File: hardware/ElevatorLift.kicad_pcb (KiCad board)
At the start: 2 copper layers, 0 parts

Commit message: Capture confirmed hardware constraints and KiCad 10 scaffold
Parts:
- added H1: MountingHole_3.2mm_M3, MountingHole_3.2mm_M3, F.Cu at (6.35, 6.35)
- added H2: MountingHole_3.2mm_M3, MountingHole_3.2mm_M3, F.Cu at (82.5, 6.35)
- added H3: MountingHole_3.2mm_M3, MountingHole_3.2mm_M3, F.Cu at (82.5, 82.5)
- added H4: MountingHole_3.2mm_M3, MountingHole_3.2mm_M3, F.Cu at (6.35, 82.5)
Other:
- board outline added: 88.9 x 88.9 mm
- board text added: "A0 placeholder outline: 3.5 in x 3.5 in"

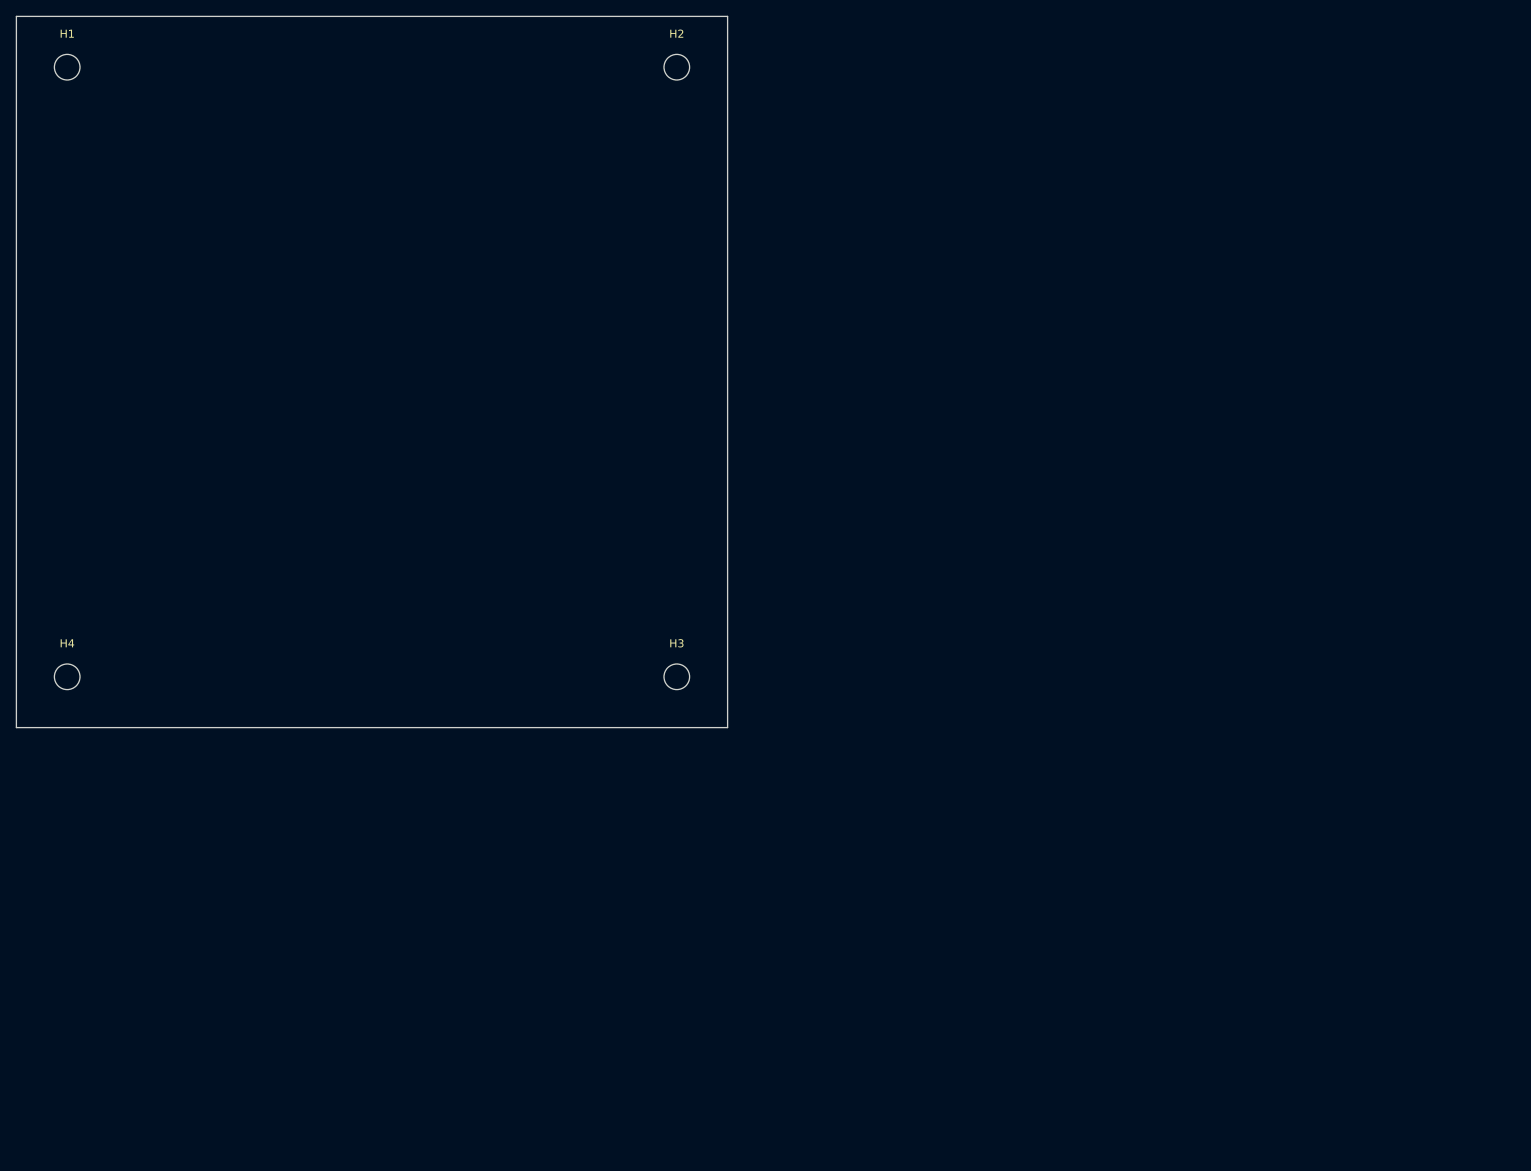
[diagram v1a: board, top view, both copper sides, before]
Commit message: Capture portable Rev-A hardware design
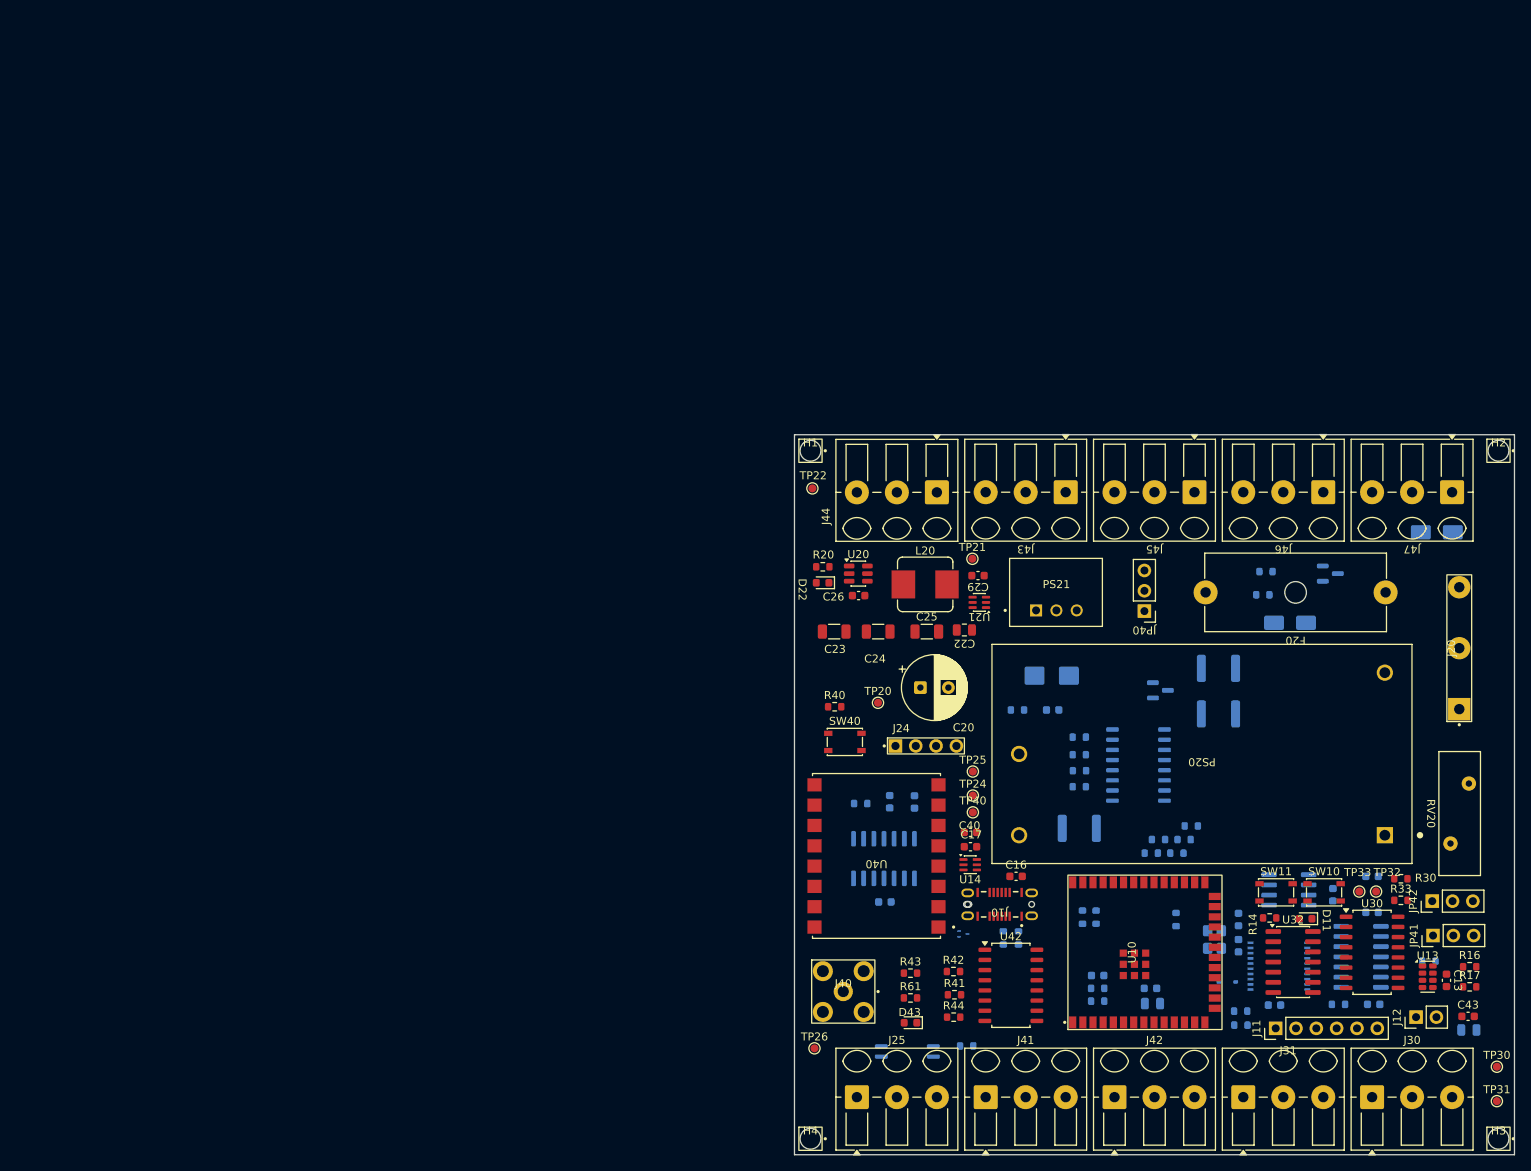
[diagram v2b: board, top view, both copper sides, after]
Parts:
- added C11: 100nF MRAM decoupling, Capacitor_SMD:C_0603_1608Metric, B.Cu at (164.6, 109.8)
- added C12: 1uF EN reset delay, Capacitor_SMD:C_0603_1608Metric, B.Cu at (135.2, 119.9)
- added C13: 100nF RTC decoupling, Capacitor_SMD:C_0603_1608Metric, F.Cu at (178.8, 120.5)
- added C14: 100nF ESP32 decoupling, Capacitor_SMD:C_0603_1608Metric, B.Cu at (141.8, 121.5)
- added C15: 10uF ESP32 bulk, Capacitor_SMD:C_0805_2012Metric, B.Cu at (142.0, 123.4)
- added C16: 1u USB IN, Capacitor_SMD:C_0603_1608Metric, F.Cu at (125.0, 107.5)
- added C17: 1u 5V OUT, Capacitor_SMD:C_0603_1608Metric, F.Cu at (119.3, 103.8)
- added C20: 100u 25V, Capacitor_THT:CP_Radial_D8.0mm_P3.50mm, F.Cu at (113.0, 83.9)
- added C21: 100n 25V, Capacitor_SMD:C_0603_1608Metric, B.Cu at (129.5, 86.7)
- added C22: 10u 10V, Capacitor_SMD:C_0805_2012Metric, F.Cu at (118.5, 76.7)
- added C23: 10u 25V, Capacitor_SMD:C_1206_3216Metric, F.Cu at (102.2, 76.9)
- added C24: 22u 10V, Capacitor_SMD:C_1206_3216Metric, F.Cu at (107.7, 76.9)
- added C25: 22u 10V, Capacitor_SMD:C_1206_3216Metric, F.Cu at (113.8, 76.9)
- added C26: 100n BST, Capacitor_SMD:C_0603_1608Metric, F.Cu at (105.3, 72.4)
- added C27: 100n 3V3, Capacitor_SMD:C_0603_1608Metric, B.Cu at (109.2, 98.2)
- added C28: 100n 5V, Capacitor_SMD:C_0603_1608Metric, B.Cu at (112.3, 98.2)
- added C29: 1uF, Capacitor_SMD:C_0603_1608Metric, F.Cu at (120.2, 69.9)
- added C30: 18pF, Capacitor_SMD:C_0603_1608Metric, B.Cu at (152.8, 116.2)
- added C31: 18pF, Capacitor_SMD:C_0603_1608Metric, B.Cu at (152.8, 112.9)
- added C32: 100nF LS7366R decoupling, Capacitor_SMD:C_0603_1608Metric, B.Cu at (157.3, 123.6)
- added C33: 100nF 74HC14 decoupling, Capacitor_SMD:C_0603_1608Metric, B.Cu at (169.7, 123.5)
- added C34: 100nF 12V FIELD DECOUPLING, Capacitor_SMD:C_0603_1608Metric, B.Cu at (169.5, 107.5)
- added C40: 100n, Capacitor_SMD:C_0603_1608Metric, F.Cu at (119.3, 102.0)
- added C41: 100n, Capacitor_SMD:C_0603_1608Metric, B.Cu at (108.6, 110.7)
- added C42: 100n, Capacitor_SMD:C_0603_1608Metric, B.Cu at (169.5, 112.0)
- added C43: 100n, Capacitor_SMD:C_0603_1608Metric, F.Cu at (181.5, 125.0)
- added C44: 10u, Capacitor_SMD:C_0805_2012Metric, B.Cu at (181.6, 126.7)
- added D11: GREEN STATUS, LED_SMD:LED_0603_1608Metric, F.Cu at (161.2, 112.8)
- added D20: SMBJ15A, Diode_SMD:D_SMB, B.Cu at (129.4, 82.4)
- added D22: 3V3 OK, LED_SMD:LED_0603_1608Metric, F.Cu at (100.8, 70.8)
- added D40: BAT54, Diode_SMD:D_SOD-323, B.Cu at (151.4, 120.7)
- added D41: SMBJ15A, Diode_SMD:D_SMA, B.Cu at (159.2, 75.8)
- added D42: SMBJ15A, Diode_SMD:D_SMA, B.Cu at (177.6, 64.5)
- added D43: RF MODE, LED_SMD:LED_0603_1608Metric, F.Cu at (111.8, 125.8)
- added F20: T500mA 250VAC + 0031.8201, Fuse:Fuseholder_Cylinder-5x20mm_Schurter_0031_8201_Horizontal_Open, F.Cu at (171.2, 72.0)
- added F21: 0.75A PTC, Fuse:Fuse_1812_4532Metric, B.Cu at (132.9, 101.5)
- added F40: 1.1A HOLD, Fuse:Fuse_1812_4532Metric, B.Cu at (150.3, 81.5)
- added F41: 500mA HOLD, Fuse:Fuse_1812_4532Metric, B.Cu at (150.3, 87.2)
- added J10: USB4145-03-0230-C_REVA2, SnapEDA:GCT_USB4145-03-0230-C_REVA2, F.Cu at (122.9, 111.0)
- added J11: UART RECOVERY / BOOT, Connector_PinHeader_2.54mm:PinHeader_1x06_P2.54mm_Vertical, F.Cu at (157.4, 126.5)
- added J12: RTC BACKUP 3V, Connector_PinHeader_2.54mm:PinHeader_1x02_P2.54mm_Vertical, F.Cu at (175.0, 125.1)
- added J20: Phoenix 1717732 GMKDS 1,5/3-7,62 MAINS L/N/PE, ElevatorLift_Custom:Phoenix_GMKDS-1.5-3-7.62_1717732_Provisional, F.Cu at (180.4, 79.0)
- added J24: VFD UART 5V GND RX TX, ElevatorLift_Custom:SAMTEC_TSW-104-07-G-S_ZeroPadded, F.Cu at (113.7, 91.2)
- added J25: ED300/3 VFD RUN C / E / SPARE, TerminalBlock_Altech:Altech_AK300_1x03_P5.00mm_45-Degree, F.Cu at (105.1, 135.1)
- added J30: ENCODER A: +12V GND A, TerminalBlock_Altech:Altech_AK300_1x03_P5.00mm_45-Degree, F.Cu at (169.5, 135.1)
- added J31: ENCODER B: +12V GND B, TerminalBlock_Altech:Altech_AK300_1x03_P5.00mm_45-Degree, F.Cu at (153.4, 135.1)
- added J40: CONSMA002 (418 MHz ANT), ElevatorLift_Custom:SMA_TE-Linx_CONSMA002_RightAngle, F.Cu at (103.4, 121.9)
- added J41: ED300/3 SAFETY HOME GND, TerminalBlock_Altech:Altech_AK300_1x03_P5.00mm_45-Degree, F.Cu at (121.2, 135.1)
- added J42: ED300/3 LIMIT UP DOWN GND, TerminalBlock_Altech:Altech_AK300_1x03_P5.00mm_45-Degree, F.Cu at (137.3, 135.1)
- added J43: ED300/3 SERVICE KEY HOLD GND, TerminalBlock_Altech:Altech_AK300_1x03_P5.00mm_45-Degree, F.Cu at (131.2, 59.5)
- added J44: ED300/3 SERVICE UP DOWN GND, TerminalBlock_Altech:Altech_AK300_1x03_P5.00mm_45-Degree, F.Cu at (115.1, 59.5)
- added J45: ED300/3 EXT LIGHT 12V / GND / SPARE, TerminalBlock_Altech:Altech_AK300_1x03_P5.00mm_45-Degree, F.Cu at (147.3, 59.5)
- added J46: ED300/3 LIGHT + / SW- / GND, TerminalBlock_Altech:Altech_AK300_1x03_P5.00mm_45-Degree, F.Cu at (163.4, 59.5)
- added J47: ED300/3 AUX + / SW- / GND, TerminalBlock_Altech:Altech_AK300_1x03_P5.00mm_45-Degree, F.Cu at (179.5, 59.5)
- added JP40: LIGHT SUPPLY SELECT, Connector_PinHeader_2.54mm:PinHeader_1x03_P2.54mm_Vertical, F.Cu at (141.0, 74.3)
- added JP41: RF BAUD0 SELECT, Connector_PinHeader_2.54mm:PinHeader_1x03_P2.54mm_Vertical, F.Cu at (177.1, 114.9)
- added JP42: RF BAUD1 SELECT, Connector_PinHeader_2.54mm:PinHeader_1x03_P2.54mm_Vertical, F.Cu at (177.0, 110.6)
- added L20: 2.2uH, Inductor_SMD:L_Bourns_SRP7028A_7.3x6.6mm, F.Cu at (113.6, 71.0)
- added PS20: RAC10-12SK/277, SnapEDA:CONV_RAC10-12SK_277, F.Cu at (148.2, 92.2)
- added PS21: R-78E5.0-0.5, SnapEDA:CONV_R-78E5.0-0.5, F.Cu at (130.0, 72.0)
- added Q40: AO3400A, Package_TO_SOT_SMD:SOT-23, B.Cu at (164.2, 69.7)
- added Q41: AO3400A, Package_TO_SOT_SMD:SOT-23, B.Cu at (143.0, 84.2)
- added R10: 5.1k 1% CC1, Resistor_SMD:R_0603_1608Metric, B.Cu at (123.4, 115.2)
- added R11: 5.1k 1% CC2, Resistor_SMD:R_0603_1608Metric, B.Cu at (125.3, 115.2)
- added R12: 10k EN pull-up, Resistor_SMD:R_0603_1608Metric, B.Cu at (135.2, 121.5)
- added R13: 10k BOOT pull-up, Resistor_SMD:R_0603_1608Metric, B.Cu at (146.9, 101.2)
- added R14: 1k STATUS LED, Resistor_SMD:R_0603_1608Metric, F.Cu at (156.7, 112.7)
- added R16: 4.7k I2C SDA pull-up, Resistor_SMD:R_0603_1608Metric, F.Cu at (181.7, 118.8)
- added R17: 4.7k I2C SCL pull-up, Resistor_SMD:R_0603_1608Metric, F.Cu at (181.7, 121.3)
- added R20: 1k, Resistor_SMD:R_0603_1608Metric, F.Cu at (100.8, 68.8)
- added R21: 0R, Resistor_SMD:R_0603_1608Metric, B.Cu at (125.1, 86.7)
- added R24: 10k OE pull-down, Resistor_SMD:R_0603_1608Metric, B.Cu at (105.5, 98.4)
- added R25: 680R, Resistor_SMD:R_0603_1608Metric, B.Cu at (118.8, 128.7)
- added R30: 2.2k ENCODER A LED, Resistor_SMD:R_0603_1608Metric, F.Cu at (173.1, 107.8)
- added R31: 2.2k ENCODER B LED, Resistor_SMD:R_0603_1608Metric, B.Cu at (176.6, 118.1)
- added R32: 10k A pull-up, Resistor_SMD:R_0603_1608Metric, B.Cu at (165.3, 123.5)
- added R33: 10k B pull-up, Resistor_SMD:R_0603_1608Metric, F.Cu at (173.1, 110.5)
- added R40: 100k, Resistor_SMD:R_0603_1608Metric, F.Cu at (102.3, 86.3)
- added R41: 2.2k, Resistor_SMD:R_0603_1608Metric, F.Cu at (117.3, 122.3)
- added R42: 2.2k, Resistor_SMD:R_0603_1608Metric, F.Cu at (117.1, 119.4)
- added R43: 2.2k, Resistor_SMD:R_0603_1608Metric, F.Cu at (111.8, 119.6)
- added R44: 2.2k, Resistor_SMD:R_0603_1608Metric, F.Cu at (117.2, 125.1)
- added R45: 2.2k, Resistor_SMD:R_0603_1608Metric, B.Cu at (132.9, 96.3)
- added R46: 2.2k, Resistor_SMD:R_0603_1608Metric, B.Cu at (132.9, 94.3)
- added R47: 2.2k, Resistor_SMD:R_0603_1608Metric, B.Cu at (132.9, 92.3)
- added R48: 2.2k, Resistor_SMD:R_0603_1608Metric, B.Cu at (132.9, 90.1)
- added R49: 10k, Resistor_SMD:R_0603_1608Metric, B.Cu at (133.3, 112.6)
- added R50: 10k, Resistor_SMD:R_0603_1608Metric, B.Cu at (135.0, 112.6)
- added R51: 10k, Resistor_SMD:R_0603_1608Metric, B.Cu at (145.0, 112.9)
- added R52: 10k, Resistor_SMD:R_0603_1608Metric, B.Cu at (135.2, 123.1)
- added R53: 10k, Resistor_SMD:R_0603_1608Metric, B.Cu at (146.0, 102.9)
- added R54: 10k, Resistor_SMD:R_0603_1608Metric, B.Cu at (145.1, 104.6)
- added R55: 10k, Resistor_SMD:R_0603_1608Metric, B.Cu at (142.8, 102.9)
- added R56: 10k, Resistor_SMD:R_0603_1608Metric, B.Cu at (141.9, 104.6)
- added R57: 100R, Resistor_SMD:R_0603_1608Metric, B.Cu at (155.8, 72.3)
- added R58: 100k, Resistor_SMD:R_0603_1608Metric, B.Cu at (156.2, 69.4)
- added R59: 100R, Resistor_SMD:R_0603_1608Metric, B.Cu at (153.0, 124.3)
- added R60: 100k, Resistor_SMD:R_0603_1608Metric, B.Cu at (153.1, 126.1)
- added R61: 1k, Resistor_SMD:R_0603_1608Metric, F.Cu at (111.8, 122.7)
- added RV20: Bourns MOV-14D241K, Varistor:RV_Disc_D15.5mm_W5.2mm_P7.5mm, F.Cu at (181.6, 95.9)
- added SW10: RESET, Button_Switch_SMD:SW_SPST_PTS810, F.Cu at (163.5, 109.5)
- added SW11: BOOT, Button_Switch_SMD:SW_SPST_PTS810, F.Cu at (157.5, 109.5)
- added SW40: RF LEARN, Button_Switch_SMD:SW_SPST_PTS810, F.Cu at (103.6, 90.7)
- added TP20: +12V TEST, TestPoint:TestPoint_Pad_D1.0mm, F.Cu at (107.7, 85.8)
- added TP21: +5V TEST, TestPoint:TestPoint_Pad_D1.0mm, F.Cu at (119.5, 67.8)
- added TP22: +3V3 TEST, TestPoint:TestPoint_Pad_D1.0mm, F.Cu at (99.5, 59.0)
- added TP24: VFD RX 5V, TestPoint:TestPoint_Pad_D1.0mm, F.Cu at (119.6, 97.4)
- added TP25: VFD TX 5V, TestPoint:TestPoint_Pad_D1.0mm, F.Cu at (119.6, 94.4)
- added TP26: VFD RUN COLLECTOR, TestPoint:TestPoint_Pad_D1.0mm, F.Cu at (99.8, 129.0)
- added TP30: ENC_A_FIELD, TestPoint:TestPoint_Pad_D1.0mm, F.Cu at (185.1, 131.3)
- added TP31: ENC_B_FIELD, TestPoint:TestPoint_Pad_D1.0mm, F.Cu at (185.1, 135.6)
- added TP32: ENC_A_CLEAN, TestPoint:TestPoint_Pad_D1.0mm, F.Cu at (170.0, 109.4)
- added TP33: ENC_B_CLEAN, TestPoint:TestPoint_Pad_D1.0mm, F.Cu at (167.9, 109.4)
- added TP40: RF RSSI, TestPoint:TestPoint_Pad_D1.0mm, F.Cu at (119.6, 99.5)
- added U10: ESP32-S3-WROOM-1U-N16R8, ElevatorLift_Custom:ESP32-S3-WROOM-1U-N16R8_CorrectedV2, F.Cu at (140.4, 117.0)
- added U11: PM004MNIATR 4Mbit MRAM, Package_SO:SOIC-8_3.9x4.9mm_P1.27mm, B.Cu at (159.1, 109.2)
- added U12: TPD2EUSB30ADRTR USB ESD, SnapEDA:SOTFL35P100X50-3N, B.Cu at (118.4, 114.7)
- added U13: RV-3028-C7 RTC, Package_SON:MicroCrystal_C7_SON-8_1.5x3.2mm_P0.9mm, F.Cu at (176.4, 120.0)
- added U14: LM66100DCKR USB IDEAL DIODE, Package_TO_SOT_SMD:SOT-363_SC-70-6, F.Cu at (119.2, 106.0)
- added U20: AP63203WU 3V3 2A, Package_TO_SOT_SMD:TSOT-23-6, F.Cu at (105.2, 69.7)
- added U21: LM66100DCKR, Package_TO_SOT_SMD:SOT-363_SC-70-6, F.Cu at (120.4, 73.2)
- added U24: TXS0104ED (3V3 <-> 5V), Package_SO:SOIC-14_3.9x8.7mm_P1.27mm, B.Cu at (108.5, 105.3)
- added U25: VFD RUN OPEN COLLECTOR, Package_SO:SOIC-4_4.55x2.6mm_P1.27mm, B.Cu at (111.4, 129.4)
- added U30: TLP291-4 ENCODER ISOLATION, Package_SO:SOIC-16_4.55x10.3mm_P1.27mm, F.Cu at (169.5, 117.0)
- added U31: 74HC14D SCHMITT CONDITIONING, Package_SO:SOIC-14_3.9x8.7mm_P1.27mm, B.Cu at (168.1, 117.6)
- added U32: LS7366R-S QUADRATURE COUNTER, Package_SO:SOIC-14_3.9x8.7mm_P1.27mm, F.Cu at (159.6, 118.2)
- added U40: RXM-418-LR, SnapEDA:XCVR_RXM-418-LR, F.Cu at (107.5, 104.9)
- added U41: LICAL-DEC-MS001, SnapEDA:20-SSOP, B.Cu at (157.8, 118.7)
- added U42: TLP291-4, Package_SO:SOIC-16_4.55x10.3mm_P1.27mm, F.Cu at (124.3, 121.1)
- added U43: TLP291-4, Package_SO:SOIC-16_4.55x10.3mm_P1.27mm, B.Cu at (140.3, 93.6)
- added Y30: 4MHz LS7366R FILTER CLOCK, Crystal:Crystal_SMD_3225-4Pin_3.2x2.5mm, B.Cu at (149.8, 115.4)
- H1, H2, H3, H4: value MountingHole_3.2mm_M3 -> Mounting Hole 2.6mm; footprint MountingHole_3.2mm_M3 -> ElevatorLift_Custom:MountingHole_2.6mm_NPTH
- moved H3 117.8 mm to (185.3, 140.3)
- moved H2 113.3 mm to (185.3, 54.3)
- moved H4 109.4 mm to (99.3, 140.3)
- moved H1 104.6 mm to (99.3, 54.3)
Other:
- board size 88.9 x 88.9 mm -> 90 x 90 mm

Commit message: Finalize Rev-A PCB preparation
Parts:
- removed D42: SMBJ15A, Diode_SMD:D_SMA
- removed F41: 500mA HOLD, Fuse:Fuse_1812_4532Metric
- removed J25: ED300/3 VFD RUN C / E / SPARE, TerminalBlock_Altech:Altech_AK300_1x03_P5.00mm_45-Degree
- removed J47: ED300/3 AUX + / SW- / GND, TerminalBlock_Altech:Altech_AK300_1x03_P5.00mm_45-Degree
- removed Q41: AO3400A, Package_TO_SOT_SMD:SOT-23
- removed R25: 680R, Resistor_SMD:R_0603_1608Metric
- removed R59: 100R, Resistor_SMD:R_0603_1608Metric
- removed R60: 100k, Resistor_SMD:R_0603_1608Metric
- removed TP26: VFD RUN COLLECTOR, TestPoint:TestPoint_Pad_D1.0mm
- removed U25: VFD RUN OPEN COLLECTOR, Package_SO:SOIC-4_4.55x2.6mm_P1.27mm
- added R62: 1k, Resistor_SMD:R_0603_1608Metric, B.Cu at (142.0, 109.5)
- J11: value UART RECOVERY / BOOT -> BOOT RESET HEADER - UART PINS 3/4 NC
- moved C23 4.67 mm to (104.8, 73.0)
- moved C26 3.49 mm to (108.2, 70.5), turned to -90 degrees
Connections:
- net VFD_ENABLE renamed VFD_COMMS_ENABLE
- J11 pad 3: /MCU_Storage/UART0_TX -> unconnected-(J11-Pin_3-Pad3)
- J11 pad 4: /MCU_Storage/UART0_RX -> unconnected-(J11-Pin_4-Pad4)
- R51 pad 1: LIMIT_UP -> Net-(R51-Pad1)
- U10 pad 15: AUX_CTRL -> SERVICE_KEY
- U10 pad 28: LIMIT_UP -> unconnected-(U10-IO35-Pad28)
- U10 pad 29: LIMIT_DOWN -> unconnected-(U10-IO36-Pad29)
- U10 pad 30: SERVICE_KEY -> unconnected-(U10-IO37-Pad30)
- U10 pad 36: /MCU_Storage/UART0_RX -> LIMIT_DOWN
- U10 pad 37: /MCU_Storage/UART0_TX -> LIMIT_UP
- U42 pad 12: LIMIT_UP -> Net-(R51-Pad1)
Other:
- copper layers 2 -> 4
